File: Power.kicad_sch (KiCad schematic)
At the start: 47 parts, among them J10 VCC, J5 GND, J6 Barrel_Jack_Switch, J8 VPP, J9 GND, Q1 BC327, Q3 BC327, U3 MCP4812, U4 LM358, U6 LM317_TO-220, U7 LM317_TO-220, U8 LM7805_TO220, U9 MC34063AP

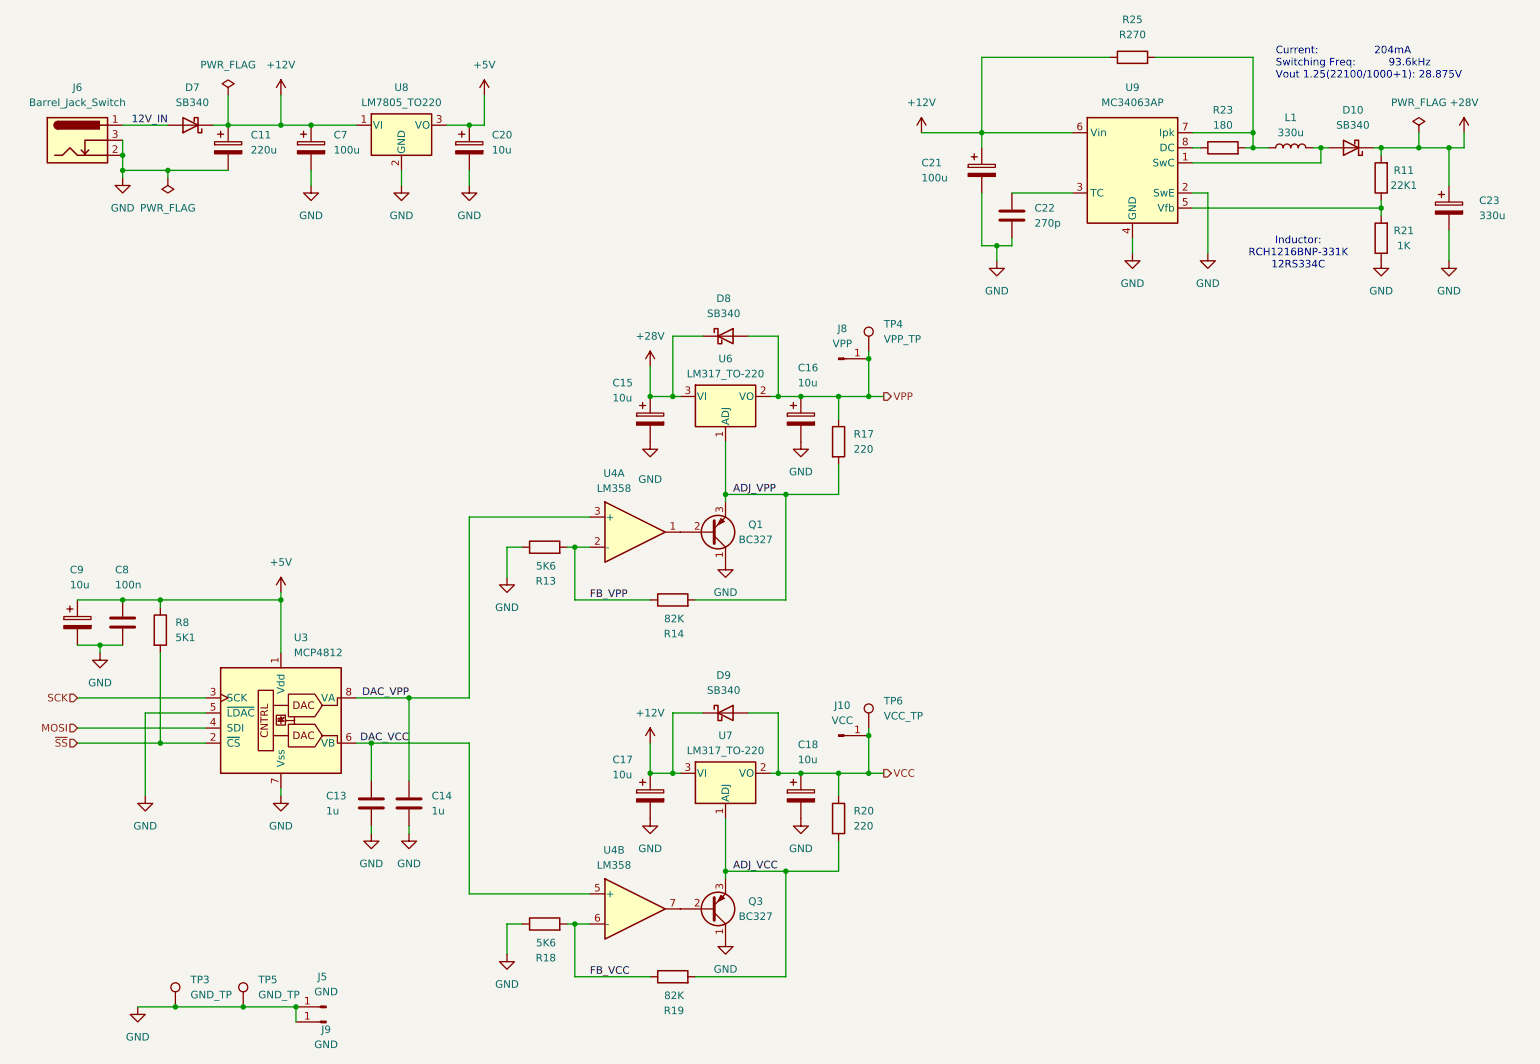
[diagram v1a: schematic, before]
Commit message: Add aditional filter for 28v line
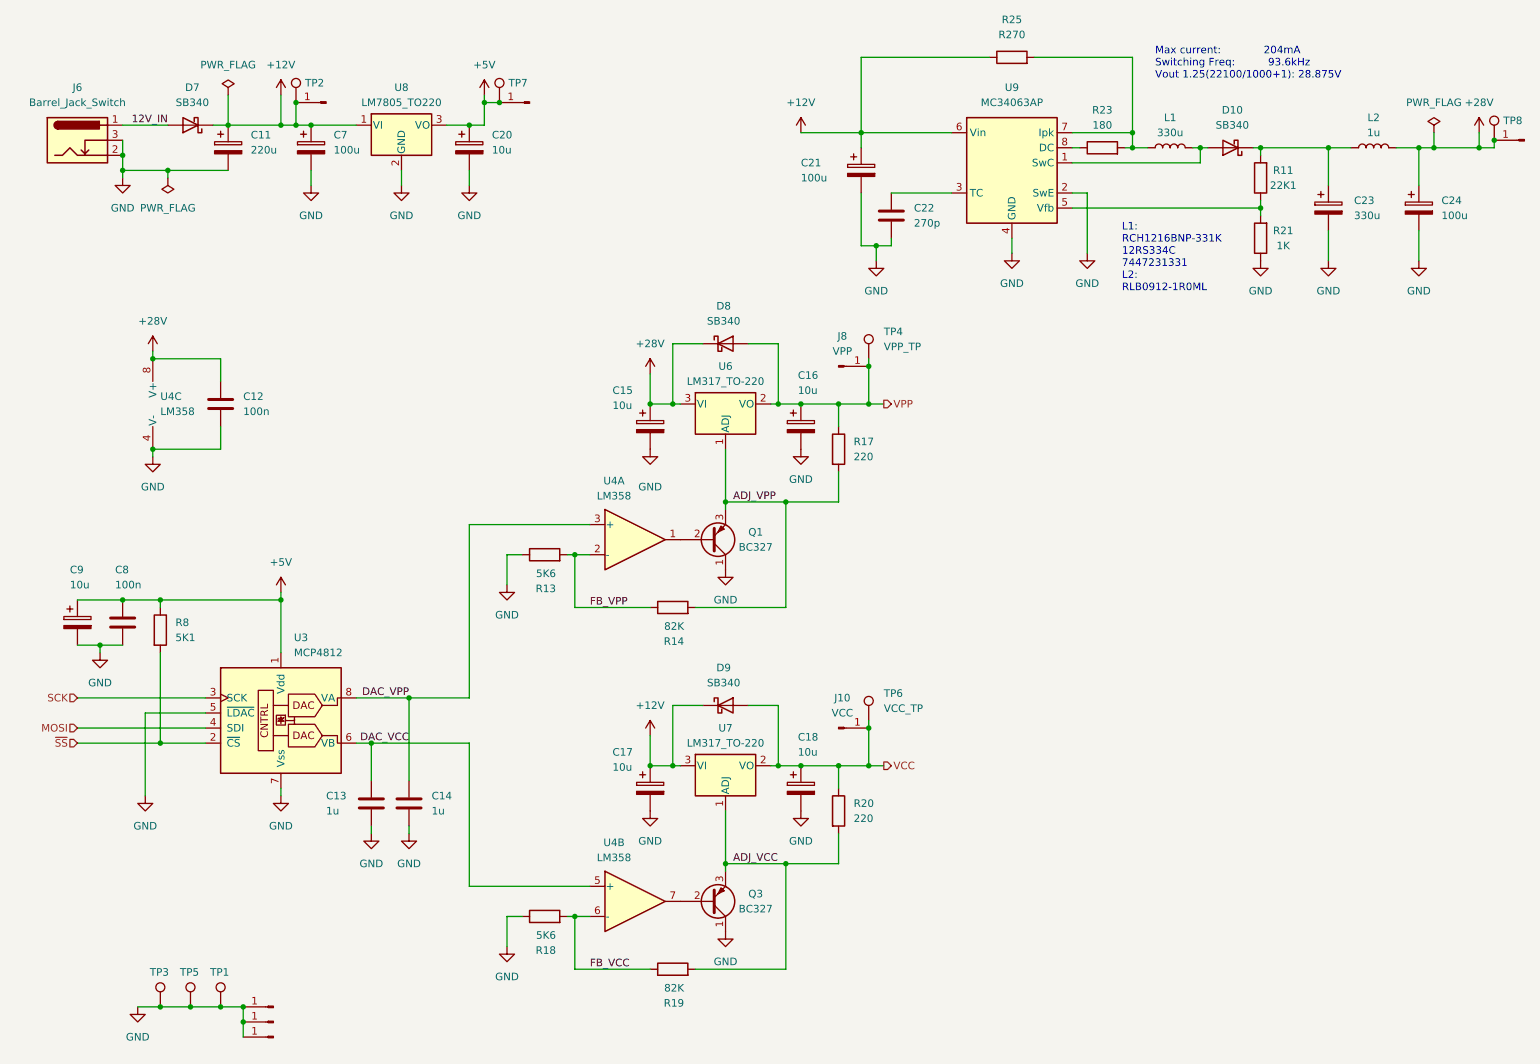
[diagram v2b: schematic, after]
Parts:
- added C12: 100n, Capacitor_THT:C_Rect_L4.6mm_W3.0mm_P2.50mm_MKS02_FKP02, symbol Device:C
- added C24: 100u, Capacitor_THT:CP_Radial_D6.3mm_P2.50mm, symbol Device:C_Polarized
- added J11: 5V, Connector_PinHeader_2.54mm:PinHeader_1x01_P2.54mm_Vertical, symbol Connector:Conn_01x01_Pin
- added J12: 28V, Connector_PinHeader_2.54mm:PinHeader_1x01_P2.54mm_Vertical, symbol Connector:Conn_01x01_Pin
- added J3: GND, Connector_PinHeader_2.54mm:PinHeader_1x01_P2.54mm_Vertical, symbol Connector:Conn_01x01_Pin
- added J4: 12V, Connector_PinHeader_2.54mm:PinHeader_1x01_P2.54mm_Vertical, symbol Connector:Conn_01x01_Pin
- added L2: 1u, Inductor_THT:L_Radial_D8.7mm_P5.00mm_Fastron_07HCP, symbol Device:L
- added TP1: GND, TestPoint:TestPoint_Pad_2.0x2.0mm, symbol Connector:TestPoint
- added TP2: 12V, TestPoint:TestPoint_Pad_2.0x2.0mm, symbol Connector:TestPoint
- added TP7: 5V, TestPoint:TestPoint_Pad_2.0x2.0mm, symbol Connector:TestPoint
- added TP8: 28V, TestPoint:TestPoint_Pad_2.0x2.0mm, symbol Connector:TestPoint
- added unit 3 of U4
- TP3, TP5: value GND_TP -> GND
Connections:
- net +12V: now also J4.1 (Pin_1), TP2.1
- net +28V: now also C12.1, C24.1, J12.1 (Pin_1), L2.2, TP8.1, U4.8 (V+); no longer C23.1, D10.1 (K), R11.2
- net +5V: now also J11.1 (Pin_1), TP7.1
- net GND: now also C12.2, C24.2, J3.1 (Pin_1), TP1.1, U4.4 (V-)
- new net: C23.1, D10.1 (K), L2.1, R11.2
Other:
- note added: "L1: RCH1216BNP-331K 12RS334C 7447231331 L2: RLB0912-1R0ML"
- note added: "Max current: 204mA Switching Freq: 93.6kHz Vout 1.25(22100/1000+1): 28.875V"
- note removed: "Current: 204mA Switching Freq: 93.6kHz Vout 1.25(22100/1000+1): 28.875V"
- note removed: "Inductor: RCH1216BNP-331K 12RS334C"
- moved on the sheet: C15, C16, C17, C18, C21, C22, C23, D10, D8, D9, J10, J8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

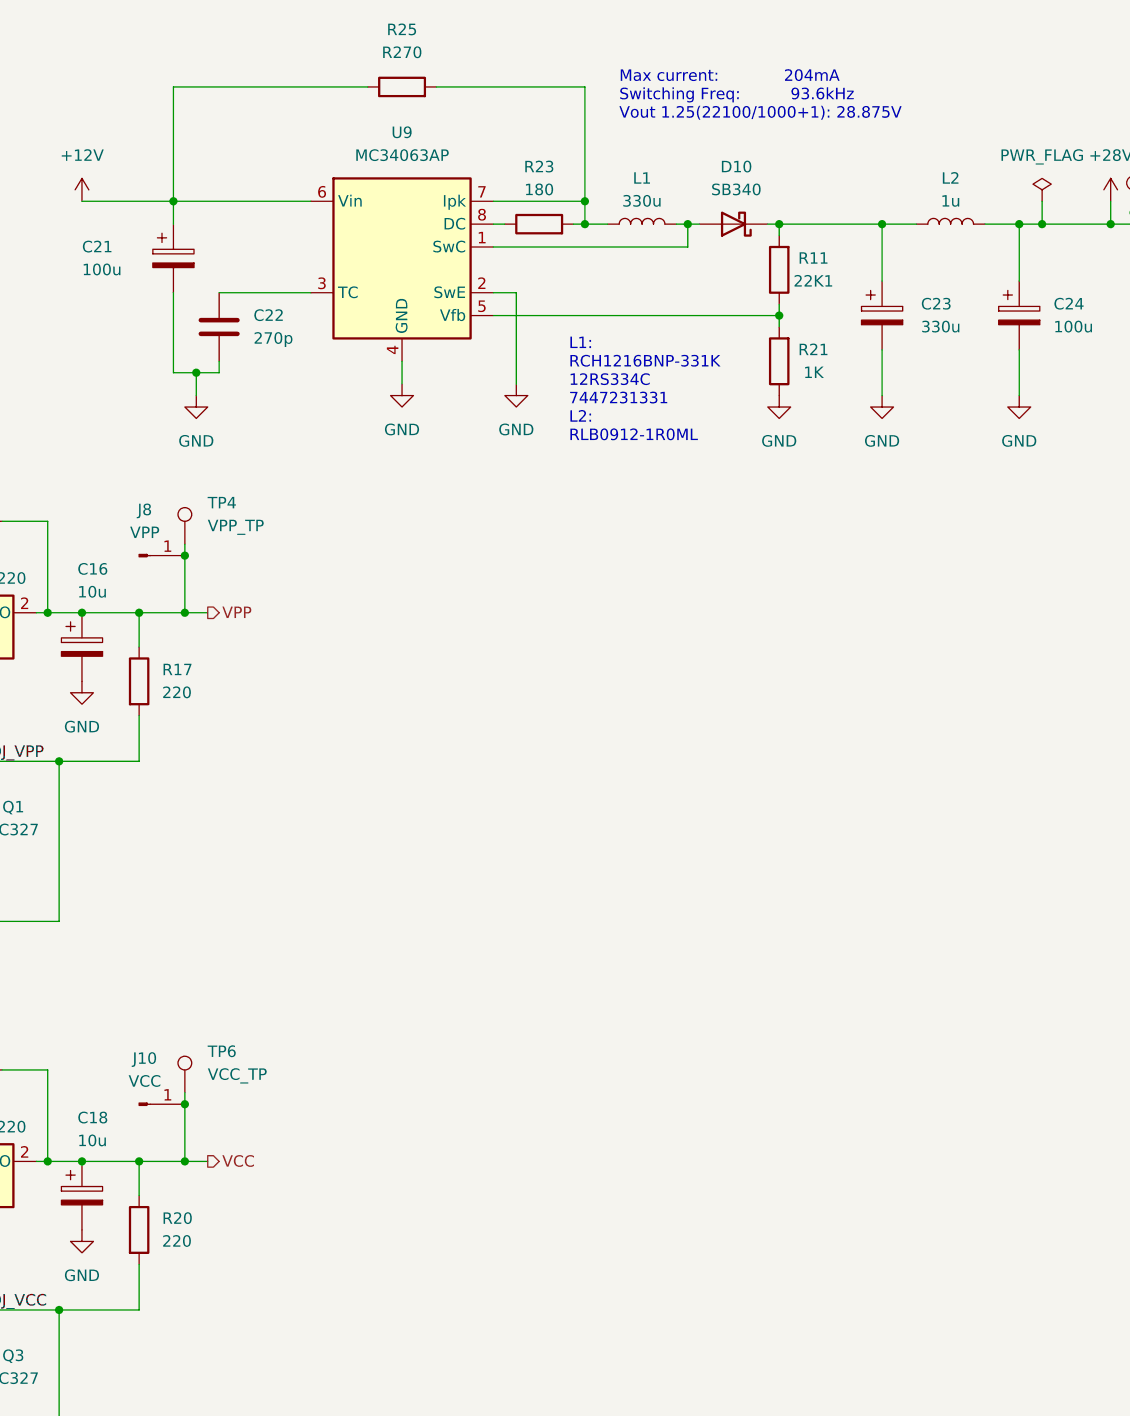
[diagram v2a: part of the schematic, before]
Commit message: Adjust component values
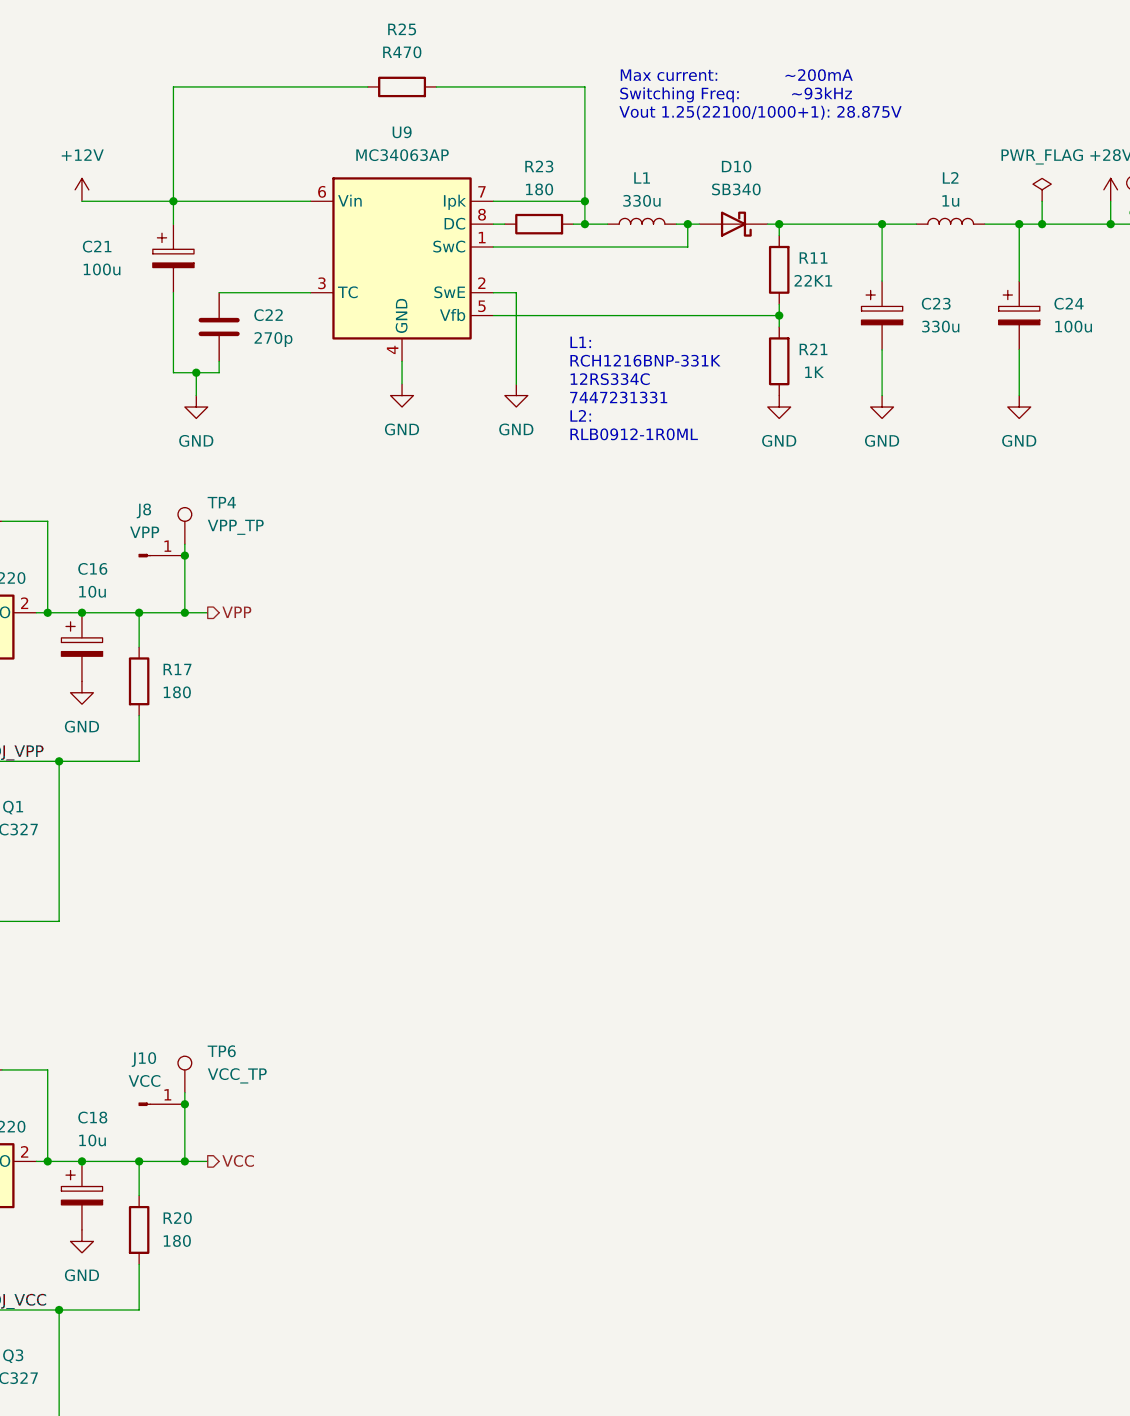
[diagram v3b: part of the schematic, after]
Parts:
- R17, R20: value 220 -> 180
- R25: value R270 -> R470
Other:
- note added: "Max current: ~200mA Switching Freq: ~93kHz Vout 1.25(22100/1000+1): 28.875V"
- note removed: "Max current: 204mA Switching Freq: 93.6kHz Vout 1.25(22100/1000+1): 28.875V"
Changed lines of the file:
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@@
 		)
 	)
-	(text "Max current:             204mA\nSwitching Freq:          93.6kHz\nVout 1.25(22100/1000+1): 28.875V"
+	(text "Max current:             ~200mA\nSwitching Freq:          ~93kHz\nVout 1.25(22100/1000+1): 28.875V"
 		(exclude_from_sim no)
 		(at 209.55 26.67 0)
@@
 			)
 		)
-		(property "Value" "R270"
+		(property "Value" "R470"
 			(at 185.42 19.05 90)
 			(effects
@@
 			)
 		)
-		(property "Value" "220"
+		(property "Value" "180"
 			(at 158.75 90.17 0)
 			(effects
@@
 			)
 		)
-		(property "Value" "220"
+		(property "Value" "180"
 			(at 158.75 151.13 0)
 			(effects

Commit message: Start working on hw revision 1.4
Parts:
- removed U7: LM317_TO-220, Package_TO_SOT_THT:TO-220-3_Vertical, symbol Regulator_Linear:LM317_TO-220
- added U7: LD1086V-DG, Package_TO_SOT_THT:TO-220-3_Vertical, symbol Regulator_Linear:LD1086V-DG
- C11: value 220u -> 470u; footprint Capacitor_THT:CP_Radial_D8.0mm_P3.50mm -> Capacitor_THT:CP_Radial_D10.0mm_P5.00mm
- C22: value 270p -> 330p
- R11: value 22K1 -> 22K
- R25: value R470 -> R330
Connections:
- net ADJ_VCC: now also U7.1 (ADJ/GND)
- net DAC_VCC: no longer C14.1, U3.8 (VA), U4.3 (+)
- net VCC: now also U7.2 (OUT)
- net +12V renamed +9V
- net +9V: now also U7.3 (IN)
- new net DAC_VPP: C14.1, U3.8 (VA), U4.3 (+)
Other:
- note added: "L1: RCH1216BNP-331K 7447231331 L2: RLB0912-1R0ML"
- note added: "Max current: ~200mA Switching Freq: ~89kHz Vout 1.25(22100/1000+1): 28.75V"
- note removed: "L1: RCH1216BNP-331K 12RS334C 7447231331 L2: RLB0912-1R0ML"
- note removed: "Max current: ~200mA Switching Freq: ~93kHz Vout 1.25(22100/1000+1): 28.875V"
- moved on the sheet: C17, C18, D9, J10, R20, TP6

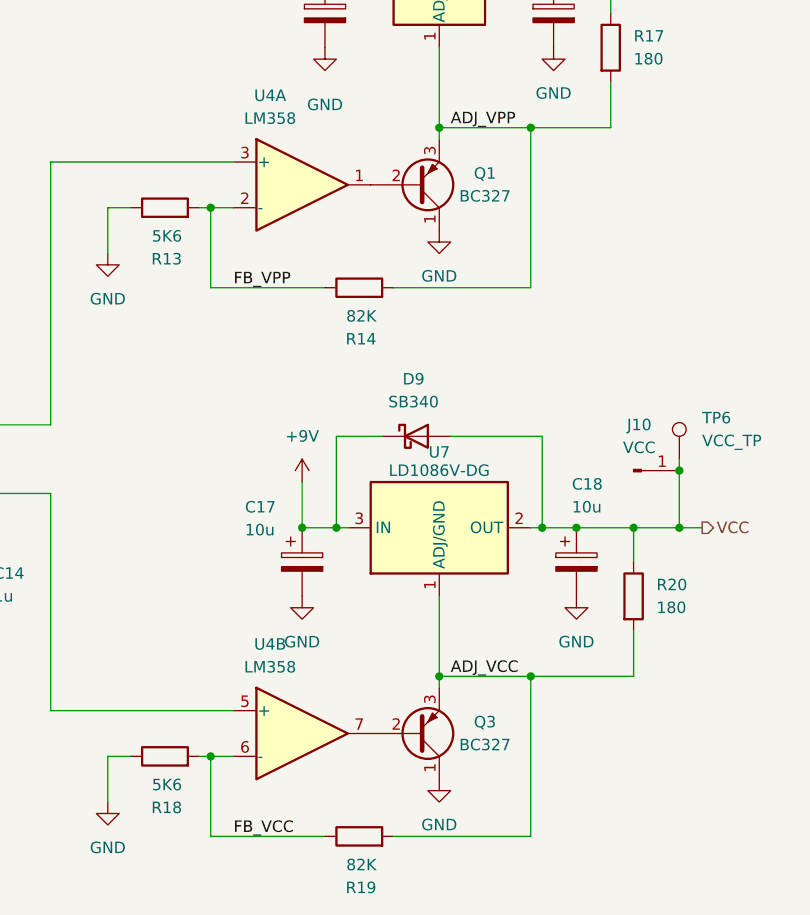
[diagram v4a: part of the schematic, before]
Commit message: Fixes after KiCad 9 upgrade
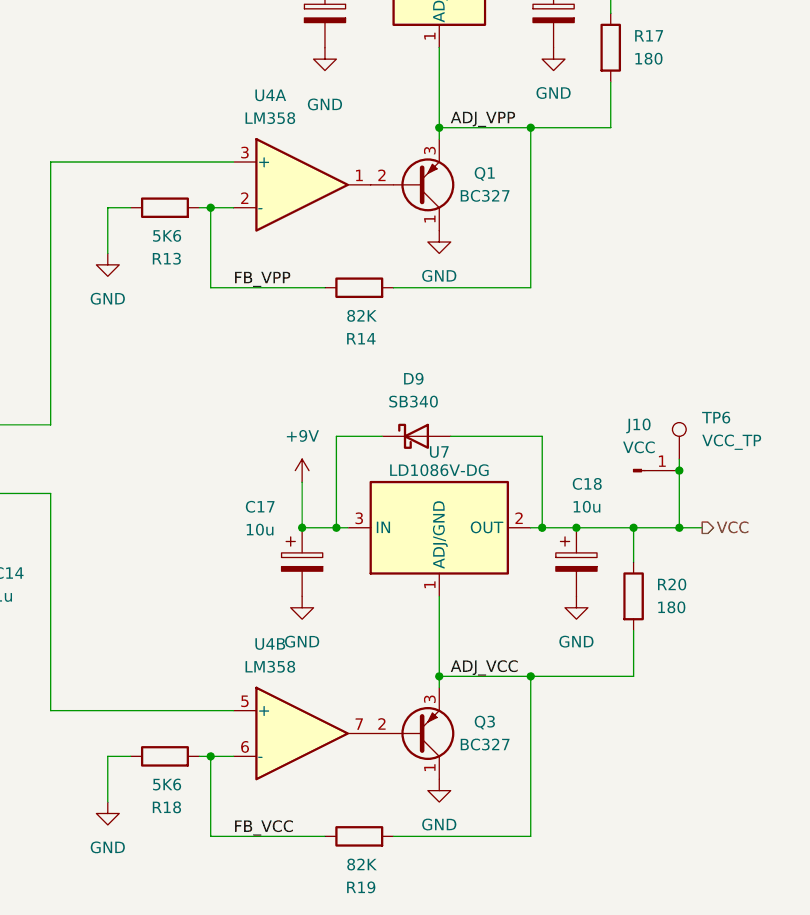
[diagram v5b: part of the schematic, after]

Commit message: Redo layout after switching to LD1086
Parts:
- U7: footprint Package_TO_SOT_THT:TO-220-3_Vertical -> Package_TO_SOT_THT:TO-220-3_Horizontal_TabDown
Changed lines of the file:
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@@
 			)
 		)
-		(property "Footprint" "Package_TO_SOT_THT:TO-220-3_Vertical"
+		(property "Footprint" "Package_TO_SOT_THT:TO-220-3_Horizontal_TabDown"
 			(at 137.16 129.54 0)
 			(effects

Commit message: Change a capacitor to a more common size
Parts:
- C23: footprint Capacitor_THT:CP_Radial_D8.0mm_P3.50mm -> Capacitor_THT:CP_Radial_D10.0mm_P5.00mm
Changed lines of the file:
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@@
 			)
 		)
-		(property "Footprint" "Capacitor_THT:CP_Radial_D8.0mm_P3.50mm"
+		(property "Footprint" "Capacitor_THT:CP_Radial_D10.0mm_P5.00mm"
 			(at 239.7252 52.07 0)
 			(effects

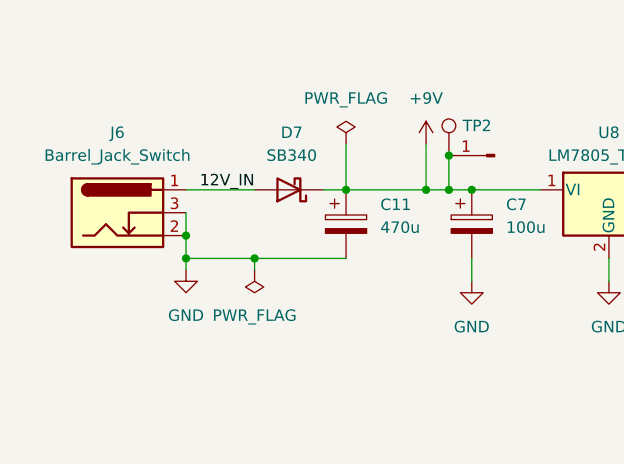
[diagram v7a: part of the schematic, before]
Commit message: Minor adjustments primarily around data diodes
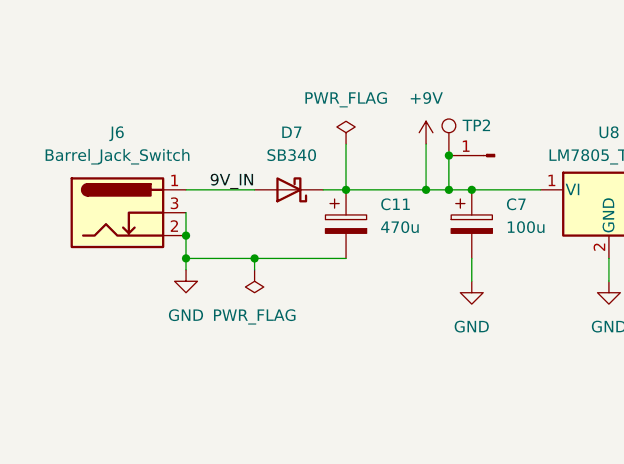
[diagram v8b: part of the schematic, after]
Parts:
- J4: value 12V -> 9V
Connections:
- net 12V_IN renamed 9V_IN
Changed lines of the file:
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@@
 		)
 	)
-	(label "12V_IN"
+	(label "9V_IN"
 		(at 43.18 34.29 180)
 		(effects
@@
 			)
 		)
-		(property "Value" "12V"
+		(property "Value" "9V"
 			(at 69.85 34.798 0)
 			(effects
